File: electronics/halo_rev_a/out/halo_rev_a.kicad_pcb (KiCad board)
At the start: 4 copper layers, 25.6 x 26 mm, 61 parts, among them J1 TC2030, J2 UWB stub, U1 nRF54L10-QFAA-R7, U2 LIS2DW12TR, X1 32.768kHz, X2 32MHz

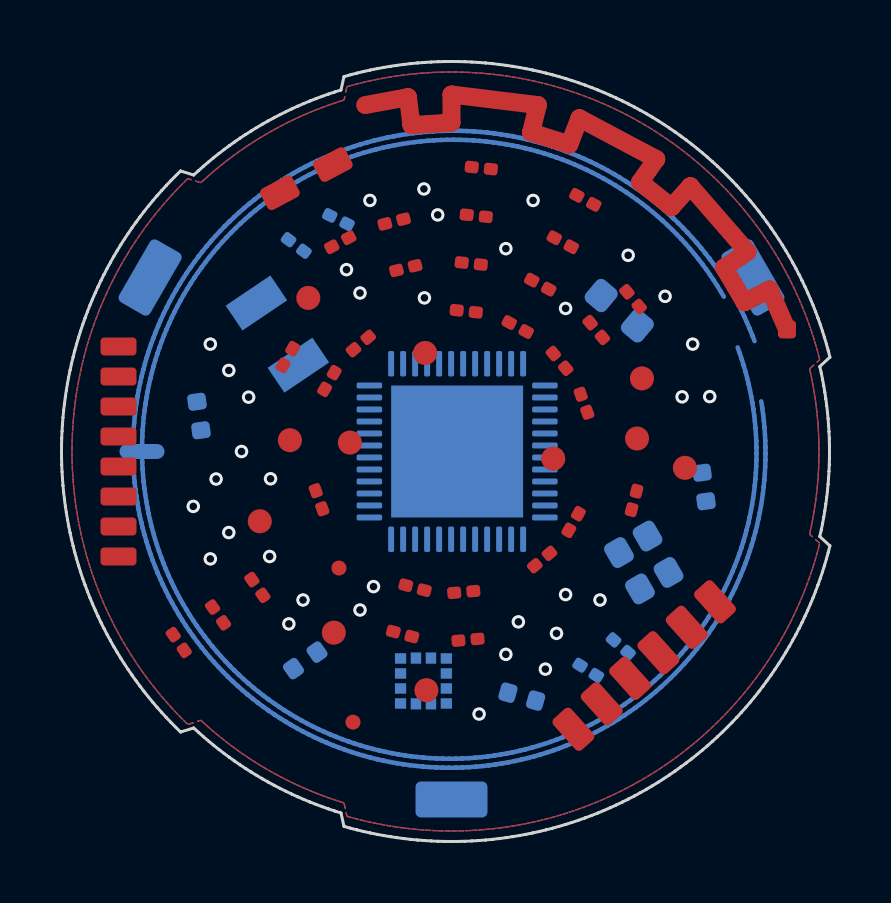
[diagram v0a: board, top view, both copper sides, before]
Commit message: B1: the net tie was 20 mm from the coil, and the plane fanout placed zero vias
Four measured defects in board.py, each found by reading the effect rather than
the log, each now carrying a check that would have caught it.

1. THE NET TIE WAS NOT ON THE COIL. `_NFC_A1_PRE` was a hand-typed copy of a
   THREE-turn winding (`20 + 360*3 - 40`) that footprints.py cut to two turns
   and never copied back, so AE2 was placed at 180 deg / R10.3167 while the
   winding's gap is at 380 deg / R10.4500 - 20 mm away on a Ø26 mm board. The
   tie tied nothing, both halves of the coil ended in mid-air, and no report
   said so. Derived from fpg.NFC_TURNS now, and the two expressions for that
   one number are asserted to agree within 0.05 mm.

2. THE WINDING HAD A HOLE IN IT. `GAP_PTS = 8` was written for a 600-chord
   spiral; the gap is now sized from a LENGTH (1.6 mm, the tie's pad pitch)
   and two stubs actually close it onto the tie's real pads, read off the
   placed footprint. Measured: NFC1 1.069 mm, NFC2 1.057 mm -> PASS.

3. THE PLANE FANOUT PLACED ZERO VIAS AND DREW ZERO STUBS. `_obstacles()` had
   no net, so every obstacle was foreign INCLUDING THE PAD THE VIA WAS BEING
   PLACED FOR: the pad's own disc reached 0.45 mm and the stub check skipped
   only its first 0.35 mm, so every pad-origin candidate collided with its own
   origin. All 35 vias that landed came from the rings, where the stub check is
   skipped - 13 VDD vias joined to nothing, 13 dangling vias, 24 unconnected
   VDD pads, and it read as a routing problem. Obstacles carry their net now;
   same-net copper is not an obstacle, it is the thing being joined.
   VDD vias 13 -> 26, GND 22 -> 40, and 42 fanout stubs exist that did not.

4. THE SPIRAL WAS 583 OF THE BOARD'S 600 TRACK SEGMENTS. The chord count is
   derived from a 5 um chord-error budget now: 208 chords, length error
   0.01521 % of the true spiral. 97 % of the autorouter's obstacle edges were
   an approximation artefact.

Also: `repair_track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
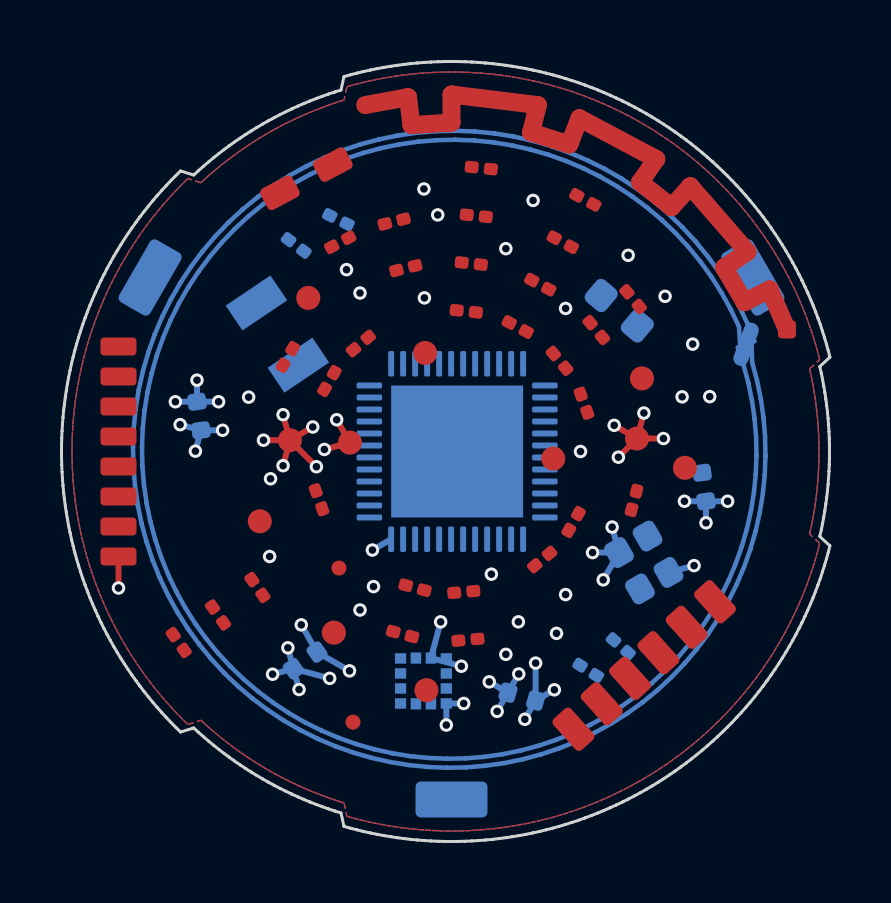
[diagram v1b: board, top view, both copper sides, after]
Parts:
- moved AE2 20.5 mm to (22.8, 9.43), turned to -110 degrees
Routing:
- net NFC1: track 0.00 -> 67.0 mm
- net NFC2: track 127.6 -> 65.1 mm
- net GND: track 0.00 -> 23.6 mm, vias 22 -> 40
- net VDD: track 0.00 -> 12.6 mm, vias 13 -> 26

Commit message: B1: a pad is a capsule, not its own diagonal — and the two tie stubs were crossed
Three more measured defects in the fanout, all in the obstacle model, none of
which announced itself.

1. A PAD WAS MODELLED AS A DISC OF ITS OWN DIAGONAL. `hypot(w, h)/2` turns a
   0.25 x 0.60 mm QFN-48 land into a disc 0.65 mm across, so its neighbour
   0.40 mm away on 0.40 mm pitch is permanently inside it and EVERY escape
   from EVERY fine-pitch pin is refused for a collision with copper that is
   not there. Measured: 16 of 24 VDD pads "unreachable", and the number did
   not move when the clearance rule was corrected — because clearance was
   never what was wrong. Pads are now COVERED by a grid of discs of radius
   min(w,h)/2 on a pitch of r*sqrt(2), which is the condition for a square
   lattice of discs to leave no gap. A capsule along the long axis was tried
   first and left the four corners out: 0.026 mm on a QFN land, 0.16 mm on
   the 3215 crystal's, and the DRC promptly found vias 0.064 mm from X1 pad 1.

2. TWO CLEARANCES, NOT ONE. Against copper the rule is min_clearance 0.127 mm;
   against another DRILL it is hole-to-hole 0.20 mm. One 0.30 mm number for
   both was applying the drill rule to every 0201 land on the board.

3. THE TIE STUBS WERE CROSSED. NFC1 to pad 1 and NFC2 to pad 2 ran each stub
   straight past the OTHER net's pad at 0.043 mm and 0.068 mm against a
   0.127 mm rule. Each coil end goes to its NEAREST tie pad now, decided by
   geometry and printed: NFC1->pad2 0.393 mm, NFC2->pad1 0.423 mm.

Also: vias were not in the obstacle list AT ALL, so the VDD stitch could not
see the 40 GND vias the GND stitch had just placed. And `link_orphans()` is
new — it joins VDD pads no via can sit beside to ones that were reached,
because a VDD pin and its own decoupling capacitor 0.5 mm away are a fanout,
not a route, and handing that to an autorouter is how VDD's 24 pins became 24
ratlines. It links 0 so far and says so by name rather than passing quietly.

MEA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
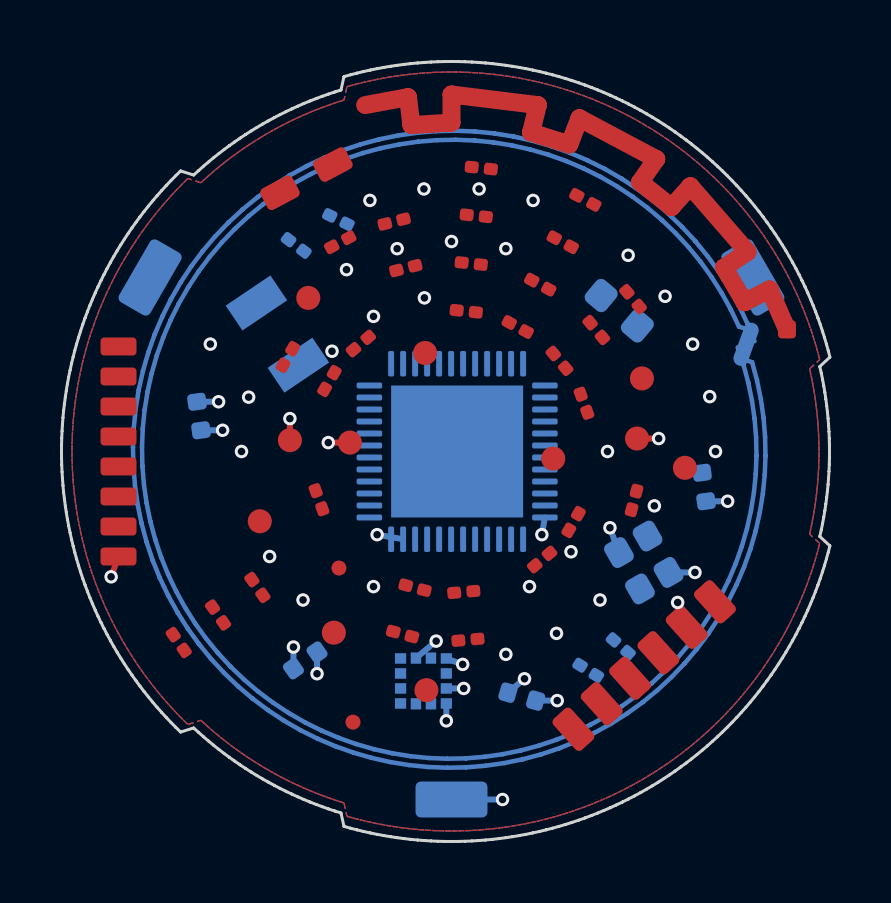
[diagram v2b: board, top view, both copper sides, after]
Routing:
- net GND: track 23.6 -> 8.42 mm
- net VDD: track 12.6 -> 7.92 mm, vias 26 -> 10
- net NFC1: track 67.0 -> 66.4 mm
- net NFC2: track 65.1 -> 64.5 mm

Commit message: B1: the crystal was out of spec, 1.1 nF does not exist, and the net tie was three times too wide
THE FOUR CHANGES FROM SOURCING AND VERIFICATION, ALL FOUR LANDED.

1. X1 IS THE WRONG CRYSTAL AND WOULD NOT HAVE STARTED. C32346 (Q13FC13500004)
   is CL = 12.5 pF, chosen on price and stock, and D-3 deletes the external
   load capacitors — so the entire load is the nRF54L's on-die caps. Nordic's
   datasheet 4503_018 v1.0 (Sept 2025) refuses 12.5 pF twice:
     * Sec 5.5.2 — OSCILLATORS.XOSC32KI.INTCAP holds 3-18 pF in 0.65 pF steps,
       and CL = (C_INT + C_pcb)/2, so the ceiling is about (18+2)/2 = 10 pF.
       12.5 pF needs C_INT ~ 23 pF: 5 pF above the hardware maximum.
     * Sec 11.9.2 — CL_LFXO min 6 pF, MAX 9 pF, at the part level, whether the
       capacitors are internal or external.
   Nordic's own reference BOM (Sec 10.3) is a CL 9 pF crystal with NO external
   load capacitors. X1 is now C95361 (Q13FC13500049), the same Epson FC-135
   body at CL 6 pF, 134,310 in stock. This is the failure the brief described:
   the crystal does not start and the board looks simply dead.

2. 1.1 nF DOES NOT EXIST, SO THE COIL MOVES INSTEAD. No 1.1 nF capacitor is
   made in 0201 in any dielectric, none in 0402, and the smallest anywhere is
   0603 — three sizes too big. C24/C25 are 1.0 nF C0G (C161371, 139,150 in
   stock) and the tank is retuned in copper, which is free: series C
   554.6 -> 500 pF, so L must rise by 554.6/500 = 1.1092, from ce-rf's
   measured 0.2449 uH to a TARGET of 0.2716 uH. footprints.py NFC_TURNS is
   DERIVED from that ratio — 2.000 -> 2.1062 turns on N-squared scaling —
   moving the innermost turn from R10.150 to R10.118, copper edge R10.043
   against the Ø20.0 cell can at R10.000. THE INDUCTANCE AT THIS LENGTH IS NOT
   MEASURED: N-squared is Wheeler's first term and ce-rf owns the solve, so
   the resonant frequency is CANNOT DETERMINE until that run exists.

3. DNP REACHES THE BOARD. The field-carry loop copied values and fields and
   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
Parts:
- added M1: , HALO_SERIAL_MARK_1X8, F.Cu at (21.8, 11.1)
- AE2: footprint NetTie-2_SMD_Pad0.5mm -> HALO_NFC_TIE_2
- C24, C25: value 1.1nF -> 1.0nF
- moved AE2 3.47 mm to (21.1, 6.42), turned to 128.883 degrees
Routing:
- net NFC1: track 66.4 -> 69.9 mm
- net NFC2: track 64.5 -> 67.8 mm
- net VDD: track 7.92 -> 7.34 mm, vias 10 -> 9
